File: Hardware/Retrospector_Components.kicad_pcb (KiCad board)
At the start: 4 copper layers, 60 x 110 mm, 145 parts, among them J1 SWD_Header, J2 Eurorack_10_pin_power, J3 Conn_01x08_Male, J4 Conn_01x08_Male, J5 Conn_01x08_Male, J6 Conn_01x08_Male, J7 USB_B_Micro, U1 STM32H743ZITx, U10 LM2675M-5, U11 TL072, U2 IS42S16800F-7TLI, U3 PCM5100APW, U4 AS3364, U5 MCP6004, U6 MCP6004, U7 TL074, U8 LD1117-3.3-4Tab, Y1 8MHz 20pF

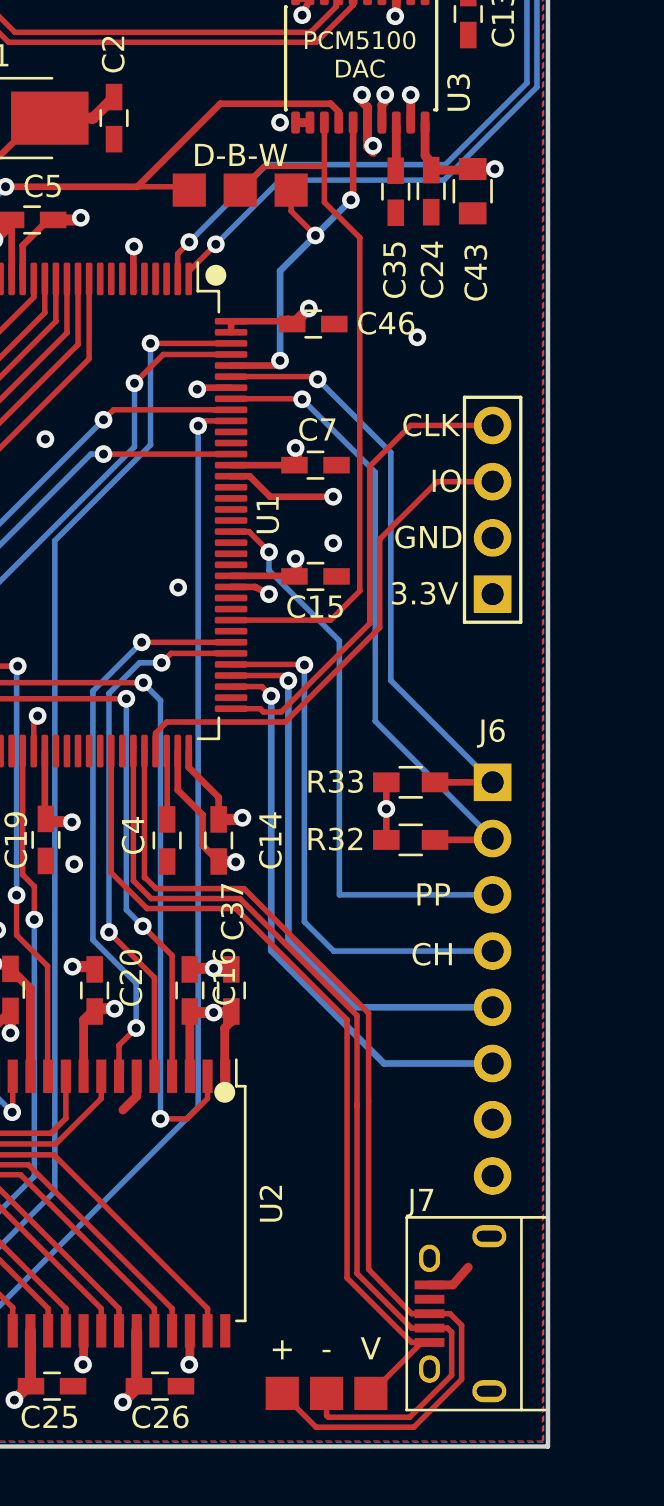
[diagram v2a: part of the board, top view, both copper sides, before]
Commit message: Schematics updated for SPI LED Driver
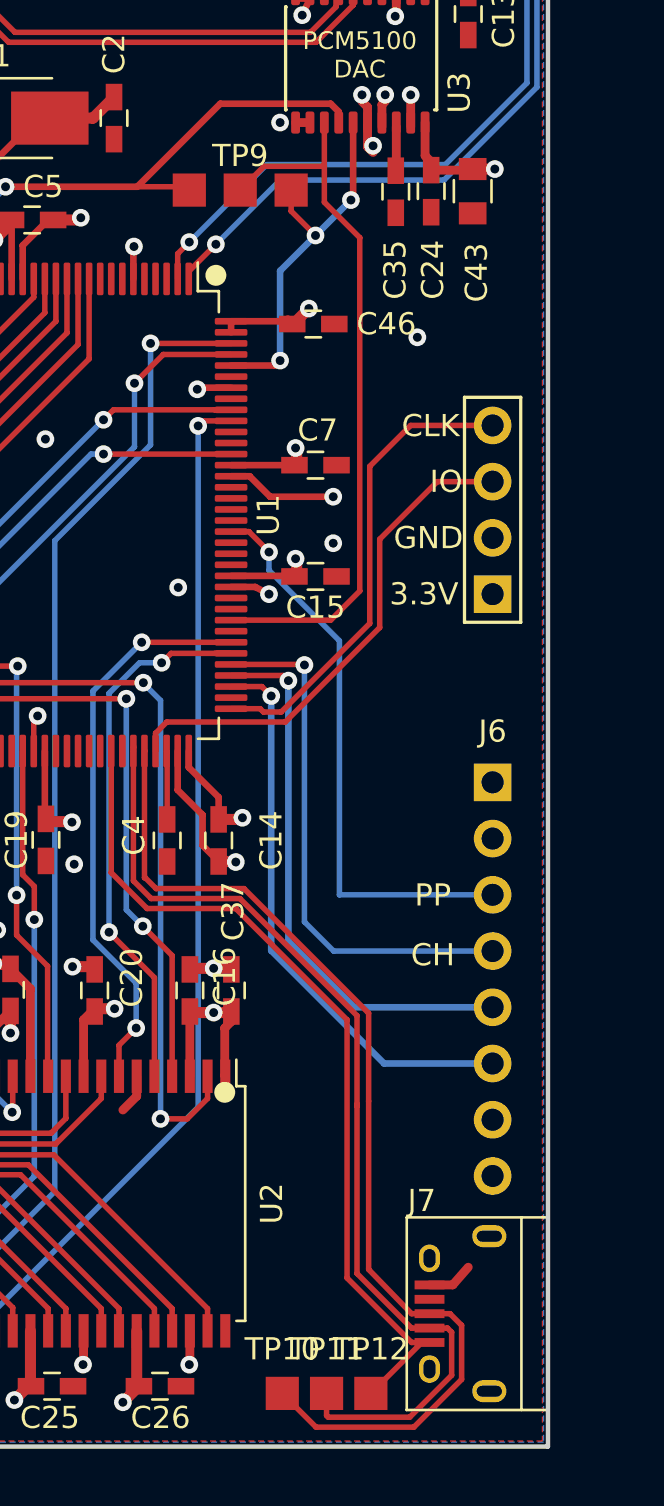
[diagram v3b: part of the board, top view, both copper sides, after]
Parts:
- removed R32, R33: 4k7, Resistors_SMD:R_0603_HandSoldering
- renumbered + to TP10, - to TP11, V to TP12, D-B-W to TP9
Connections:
- J6 pad 1: /LED_I2C_CLK -> /LED_SPI_CLK
- J6 pad 2: /LED_I2C_DATA -> /LED_SPI_DATA
- U1 pad 137: /LED_I2C_DATA -> Net-(U1-Pad137)
- U1 pad 139: /LED_I2C_CLK -> Net-(U1-Pad139)
- U1 pad 19: Net-(U1-Pad19) -> /LED_SPI_CLK
- U1 pad 21: Net-(U1-Pad21) -> /LED_SPI_DATA
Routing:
- net /LED_I2C_DATA: track 29.3 -> 0.00 mm, vias 1 -> 0
- net /LED_I2C_CLK: track 28.1 -> 0.00 mm, vias 1 -> 0
- net +3V3: track 119.1 -> 116.5 mm, vias 21 -> 20

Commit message: Work on PCB routing
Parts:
- moved C53 71.0 mm to (112.7, 91.9), turned to 180 degrees
- moved R13 1.80 mm to (123.4, 95.0)
- moved R9 1.80 mm to (121.6, 95.0)
- moved C31 0.61 mm to (153.9, 90.9)
- turned C29 to 90 degrees
- turned R12 to 90 degrees
- turned R24 to 90 degrees
- turned R26 to 90 degrees
- turned R8 to 90 degrees
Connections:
- J3 pad 3: /EXT_AUDIO_IN_L -> /DELAY_CV_L
- J3 pad 4: /EXT_AUDIO_IN_R -> /DELAY_CV_R
- J3 pad 5: /DELAY_CV_L -> /EXT_AUDIO_IN_L
- J3 pad 6: /DELAY_CV_R -> /EXT_AUDIO_IN_R
- J3 pad 7: /RESET -> /DELAY_POT_R
- J5 pad 6: /DELAY_POT_R -> /RESET
- J6 pad 1: /LED_SPI_CLK -> /LED_SPI_DATA
- J6 pad 2: /LED_SPI_DATA -> /LED_SPI_CLK
- U1 pad 128: Net-(U1-Pad128) -> /LED_SPI_CLK
- U1 pad 129: Net-(U1-Pad129) -> /LED_SPI_DATA
- U1 pad 19: /LED_SPI_CLK -> Net-(U1-Pad19)
- U1 pad 21: /LED_SPI_DATA -> Net-(U1-Pad21)
- U1 pad 36: /AUDIO_IN_L -> /AUDIO_IN_R
- U1 pad 37: /AUDIO_IN_R -> /AUDIO_IN_L
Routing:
- net /TONE_POT: track 1.51 -> 48.6 mm
- net /DELAY_POT_R: track 0.00 -> 47.0 mm, vias 0 -> 1
- net /RESET: track 0.00 -> 42.2 mm, vias 0 -> 1
- net /DELAY_CV_R: track 0.00 -> 36.6 mm, vias 0 -> 1
- net /DELAY_CV_L: track 0.00 -> 32.8 mm
- net /AUDIO_IN_L: track 4.40 -> 28.4 mm
- net /LED_SPI_CLK: track 0.00 -> 21.3 mm, vias 0 -> 1
- net /LED_SPI_DATA: track 0.00 -> 20.3 mm, vias 0 -> 1
- net /AUDIO_IN_R: track 4.70 -> 22.7 mm
- net VCC: track 66.0 -> 83.4 mm, vias 1 -> 3
- net +3.3VA: track 16.9 -> 34.1 mm, vias 3 -> 6
- net /EXT_AUDIO_IN_R: track 36.3 -> 28.7 mm
- net /EXT_AUDIO_IN_L: track 40.4 -> 33.9 mm
- net GND: track 68.5 -> 74.1 mm, vias 45 -> 52
- net /DELAY_CV_SCALED_R: track 13.7 -> 16.4 mm, vias 0 -> 2
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
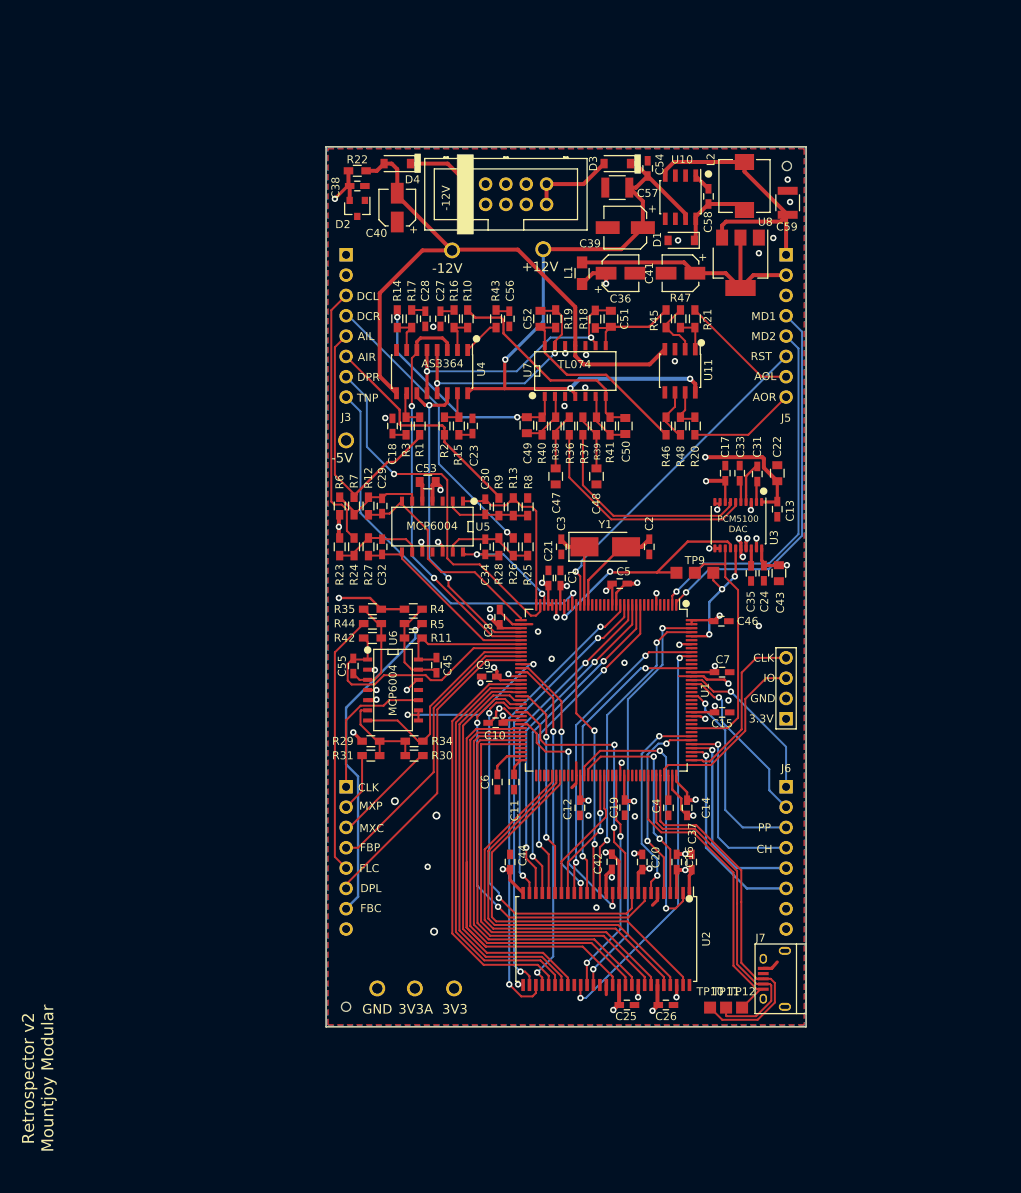
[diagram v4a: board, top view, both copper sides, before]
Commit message: Completed routing pass of PCB
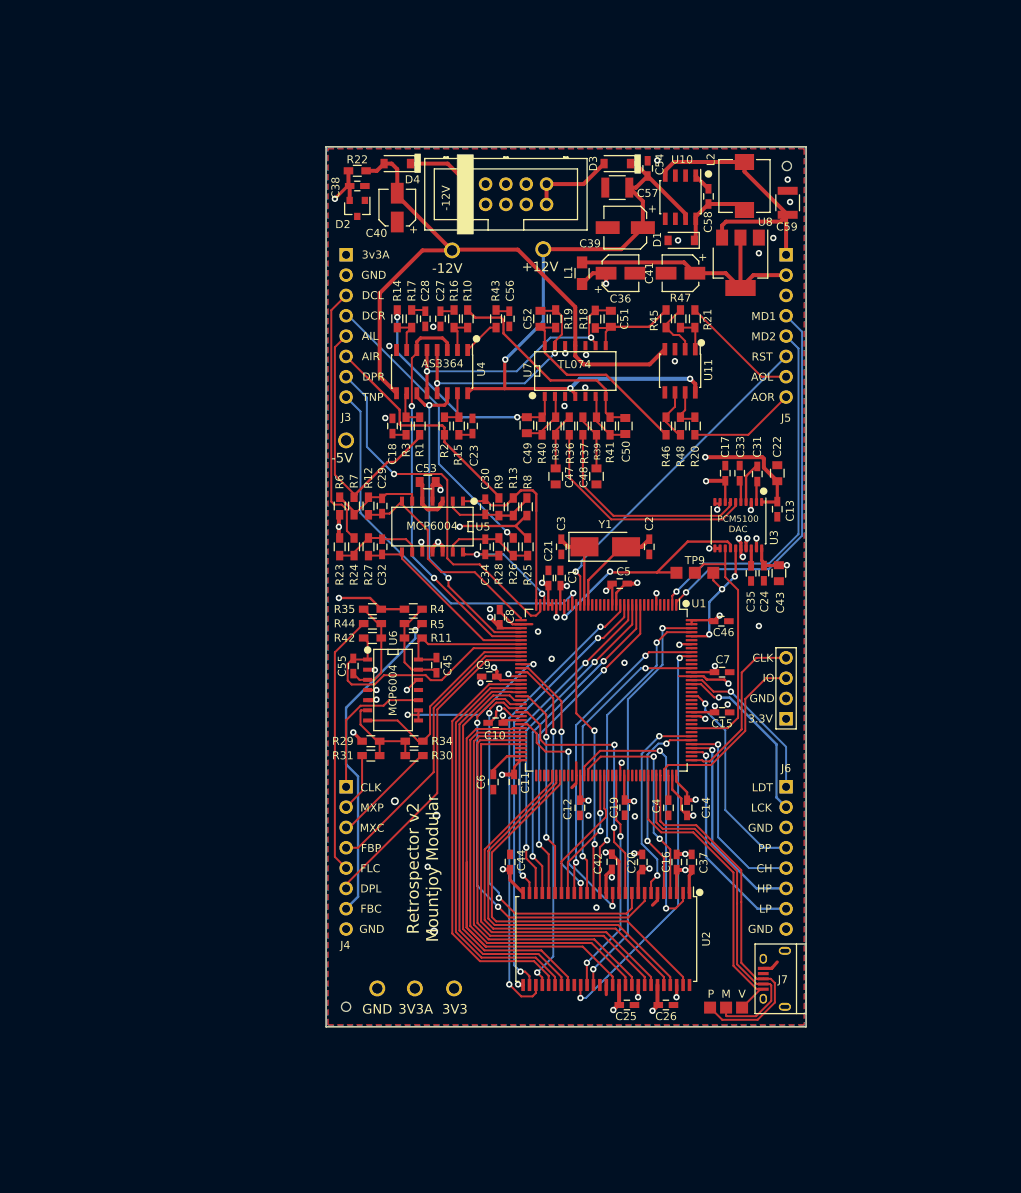
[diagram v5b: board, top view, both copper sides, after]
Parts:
- moved C6 0.50 mm to (120.9, 129.4)
- moved R8 0.10 mm to (125.1, 95.0), turned to 270 degrees
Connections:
- J6 pad 3: /PINGPONG -> GND
- J6 pad 4: /CHORUS -> /PINGPONG
- J6 pad 5: /HP_MODE -> /CHORUS
- J6 pad 6: /LP_MODE -> /HP_MODE
- J6 pad 7: +3.3VA -> /LP_MODE
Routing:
- net /-5V_REF: track 89.6 -> 115.8 mm, vias 4 -> 5
- net GND: track 74.1 -> 80.1 mm, vias 52 -> 54
- net /AUDIO_IN_R: track 22.7 -> 24.7 mm
- net /LP_MODE: track 25.6 -> 27.4 mm
- net +3V3: track 116.5 -> 118.3 mm, vias 20 -> 21
- net /CHORUS: track 24.0 -> 25.1 mm
- net /PINGPONG: track 24.9 -> 26.0 mm
- net /HP_MODE: track 25.0 -> 26.0 mm
- net /LED_SPI_CLK: track 21.3 -> 22.1 mm
- net Net-(C30-Pad2): track 10.9 -> 11.7 mm
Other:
- board text added: "3v3A"
- board text added: "HP"
- board text added: "J4"
- board text added: "LCK"
- board text added: "LDT"
- board text added: "LP"
- board text added: "M"
- board text added: "P"
- board text added: "To Do: Thermal Vias on LDO Ground Vias Opamp decoupling caps Ground under MCU/RAM"
- board text added: "V"

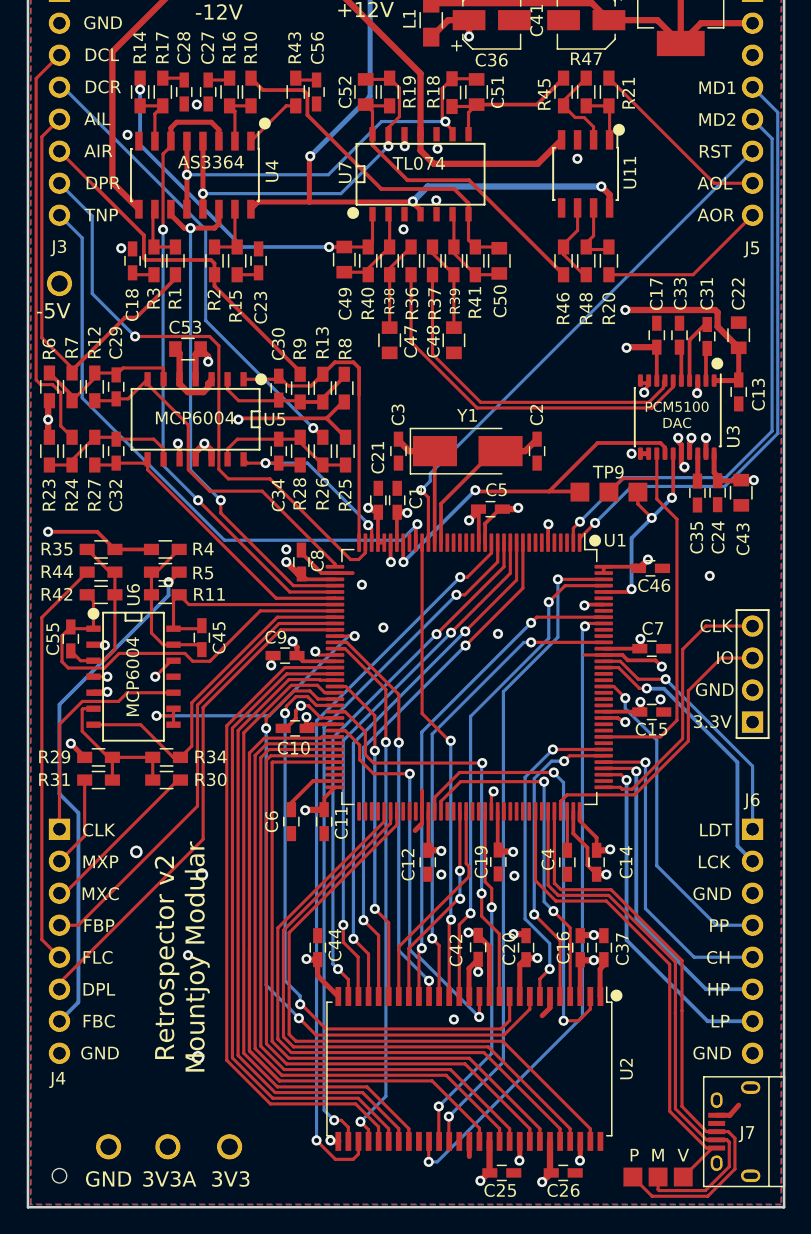
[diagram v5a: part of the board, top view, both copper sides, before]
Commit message: Started length matching RAM traces
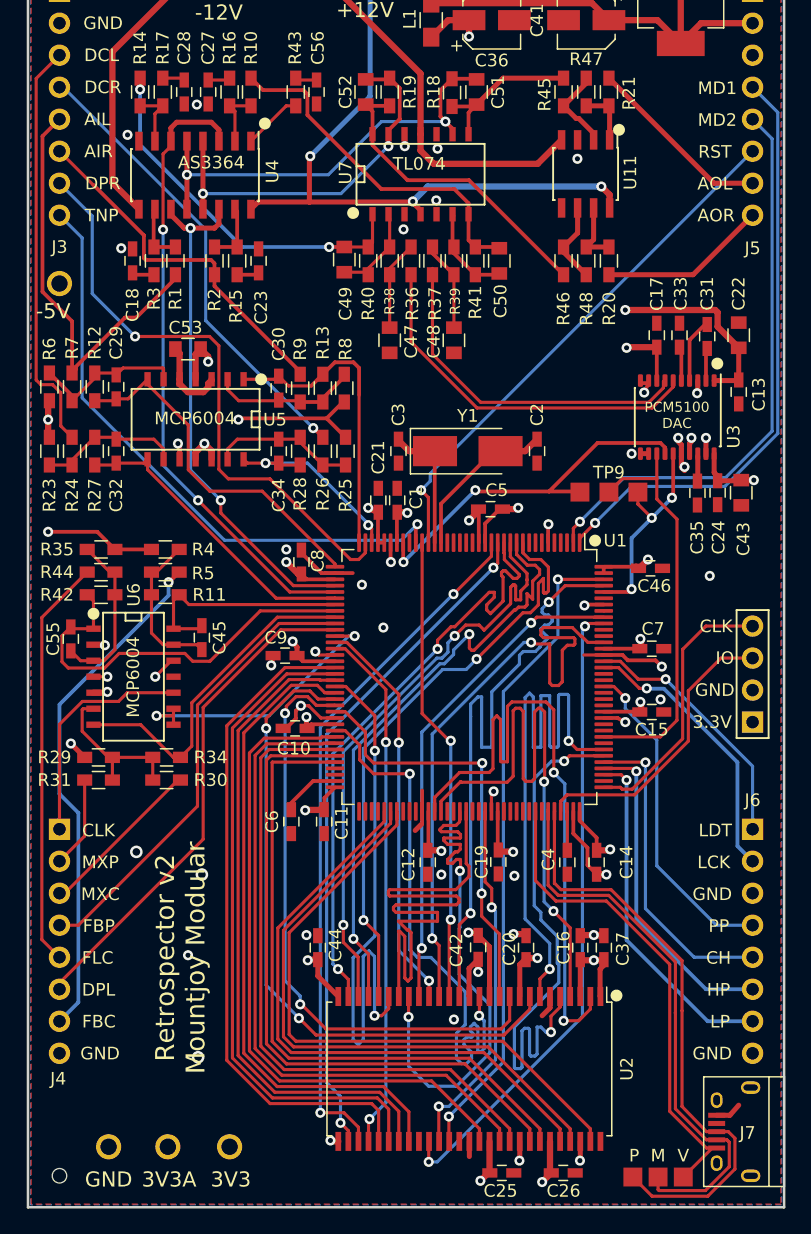
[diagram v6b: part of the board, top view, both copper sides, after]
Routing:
- net /FMC_BA1: track 17.1 -> 46.2 mm
- net /FMC_D3: track 25.7 -> 51.5 mm
- net /FMC_BA0: track 16.5 -> 41.0 mm
- net /FMC_D1: track 26.8 -> 49.1 mm
- net /FMC_D2: track 24.4 -> 45.0 mm
- net /FMC_A10: track 26.9 -> 46.6 mm
- net /FMC_D0: track 34.9 -> 52.4 mm
- net /FMC_D7: track 31.4 -> 46.3 mm
- net /FMC_~CAS: track 37.7 -> 50.6 mm
- net /FMC_D8: track 64.3 -> 52.8 mm
- net /FMC_~BL0: track 39.1 -> 49.8 mm
- net /FMC_A3: track 42.1 -> 49.1 mm
- net /FMC_A0: track 41.7 -> 47.8 mm
- net /FMC_A1: track 41.9 -> 47.9 mm
- net /FMC_A2: track 42.0 -> 47.5 mm
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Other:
- board text added: "To Do: Thermal Vias on LDO Ground Vias Opamp decoupling caps Ground under MCU/RAM Layer indicator Widen traces Length match RAM"
- board text removed: "To Do: Thermal Vias on LDO Ground Vias Opamp decoupling caps Ground under MCU/RAM"
